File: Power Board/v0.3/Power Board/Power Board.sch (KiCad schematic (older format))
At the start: 3 parts, among them J1 Battery In, J2 Conn_01x06, SW1 SW_Push

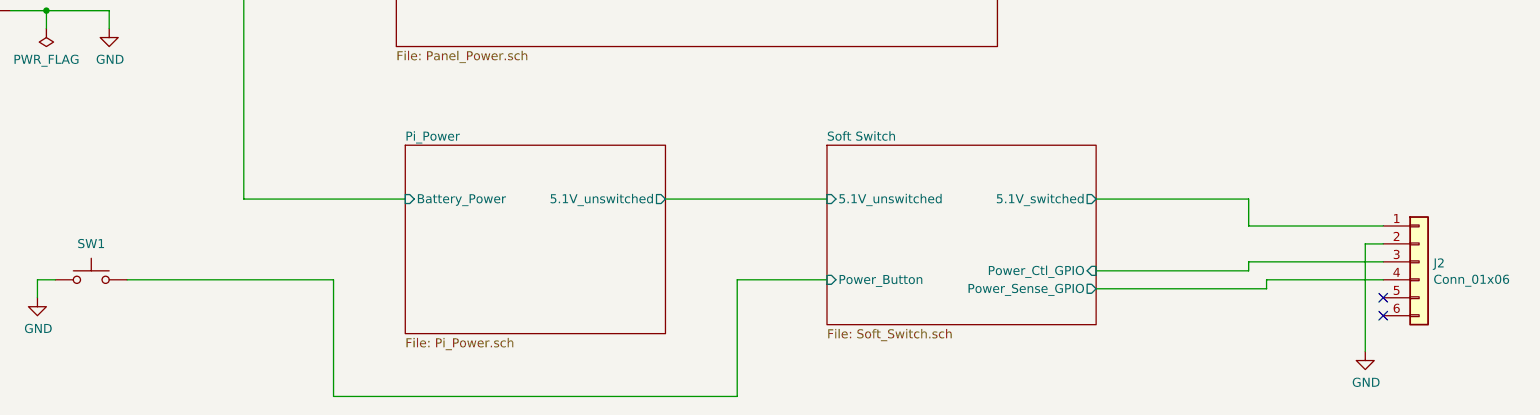
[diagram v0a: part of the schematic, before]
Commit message: Revised soft power switch.  Now switches power to 5V regulator.
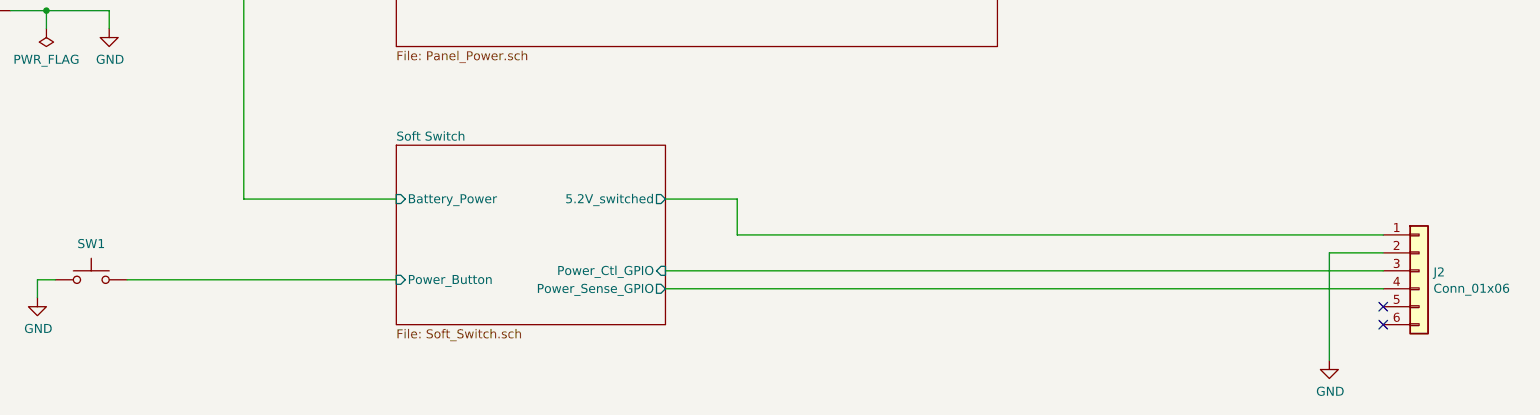
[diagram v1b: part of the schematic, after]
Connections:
- net Pi_Power/Battery_Power renamed Soft Switch/Battery_Power
- net Soft Switch/5.1V_switched renamed Soft Switch/5.2V_switched
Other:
- moved on the sheet: J2
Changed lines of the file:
@@
 	1    0    0    -1
 $EndComp
-$Sheet
-S 4150 3600 1450 1050
-U 5C93509D
-F0 "Pi_Power" 50
-F1 "Pi_Power.sch" 50
-F2 "Battery_Power" I L 4150 3900 50
-F3 "5.1V_unswitched" O R 5600 3900 50
-$EndSheet
-$Sheet
-S 6500 3600 1500 1000
-U 5C958DBD
-F0 "Soft Switch" 50
-F1 "Soft_Switch.sch" 50
-F2 "5.1V_unswitched" I L 6500 3900 50
-F3 "5.1V_switched" O R 8000 3900 50
-F4 "Power_Ctl_GPIO" I R 8000 4300 50
-F5 "Power_Sense_GPIO" O R 8000 4400 50
-F6 "Power_Button" I L 6500 4350 50
-$EndSheet
 $Comp
 L power:PWR_FLAG #FLG02
@@
 Wire Wire Line
 	3250 2750 3250 3900
-Wire Wire Line
-	3250 3900 4150 3900
 Connection ~ 2150 2750
 $Comp
@@
 Wire Wire Line
 	2100 4350 2100 4450
-Wire Wire Line
-	2600 4350 3750 4350
-Wire Wire Line
-	3750 4350 3750 5000
-Wire Wire Line
-	3750 5000 6000 5000
-Wire Wire Line
-	6000 5000 6000 4350
-Wire Wire Line
-	6000 4350 6500 4350
-Wire Wire Line
-	6500 3900 5600 3900
 $Comp
 L Connector_Generic:Conn_01x06 J2
 U 1 1 5C997D7E
-P 9800 4250
-F 0 "J2" H 9880 4242 50  0000 L CNN
-F 1 "Conn_01x06" H 9880 4151 50  0000 L CNN
-F 2 "" H 9800 4250 50  0001 C CNN
-F 3 "~" H 9800 4250 50  0001 C CNN
-F 4 "WM4904-ND" H 0   0   50  0001 C CNN "Digikey No."
-F 5 "Molex" H 0   0   50  0001 C CNN "Manufacturer"
-F 6 "70553-0005" H 0   0   50  0001 C CNN "Part No."
-	1    9800 4250
+P 9800 4300
+F 0 "J2" H 9880 4292 50  0000 L CNN
+F 1 "Conn_01x06" H 9880 4201 50  0000 L CNN
+F 2 "" H 9800 4300 50  0001 C CNN
+F 3 "~" H 9800 4300 50  0001 C CNN
+F 4 "WM4904-ND" H 0   50  50  0001 C CNN "Digikey No."
+F 5 "Molex" H 0   50  50  0001 C CNN "Manufacturer"
+F 6 "70553-0005" H 0   50  50  0001 C CNN "Part No."
+	1    9800 4300
 	1    0    0    -1
 $EndComp
 Wire Wire Line
-	9600 4050 8850 4050
+	9600 4100 6000 4100
 Wire Wire Line
-	8850 4050 8850 3900
+	9600 4200 9300 4200
 Wire Wire Line
-	8850 3900 8000 3900
-Wire Wire Line
-	8000 4300 8850 4300
-Wire Wire Line
-	8850 4300 8850 4250
-Wire Wire Line
-	8850 4250 9600 4250
-Wire Wire Line
-	8000 4400 8950 4400
-Wire Wire Line
-	8950 4400 8950 4350
-Wire Wire Line
-	8950 4350 9600 4350
-Wire Wire Line
-	9600 4150 9500 4150
-Wire Wire Line
-	9500 4150 9500 4750
+	9300 4200 9300 4800
 $Comp
 L power:GND #PWR03
 U 1 1 5C99AE97
-P 9500 4750
-F 0 "#PWR03" H 9500 4500 50  0001 C CNN
-F 1 "GND" H 9505 4577 50  0000 C CNN
-F 2 "" H 9500 4750 50  0001 C CNN
-F 3 "" H 9500 4750 50  0001 C CNN
-	1    9500 4750
+P 9300 4800
+F 0 "#PWR03" H 9300 4550 50  0001 C CNN
+F 1 "GND" H 9305 4627 50  0000 C CNN
+F 2 "" H 9300 4800 50  0001 C CNN
+F 3 "" H 9300 4800 50  0001 C CNN
+	1    9300 4800
 	1    0    0    -1
 $EndComp
-NoConn ~ 9600 4450
-NoConn ~ 9600 4550
+NoConn ~ 9600 4500
+NoConn ~ 9600 4600
+Wire Wire Line
+	6000 4100 6000 3900
+Wire Wire Line
+	6000 3900 5600 3900
+Wire Wire Line
+	5600 4400 9600 4400
+Wire Wire Line
+	9600 4300 5600 4300
+Wire Wire Line
+	4100 3900 3250 3900
+Wire Wire Line
+	2600 4350 4100 4350
+$Sheet
+S 4100 3600 1500 1000
+U 5C958DBD
+F0 "Soft Switch" 50
+F1 "Soft_Switch.sch" 50
+F2 "Power_Ctl_GPIO" I R 5600 4300 50
+F3 "Power_Sense_GPIO" O R 5600 4400 50
+F4 "Power_Button" I L 4100 4350 50
+F5 "5.2V_switched" O R 5600 3900 50
+F6 "Battery_Power" I L 4100 3900 50
+$EndSheet
 $EndSCHEMATC

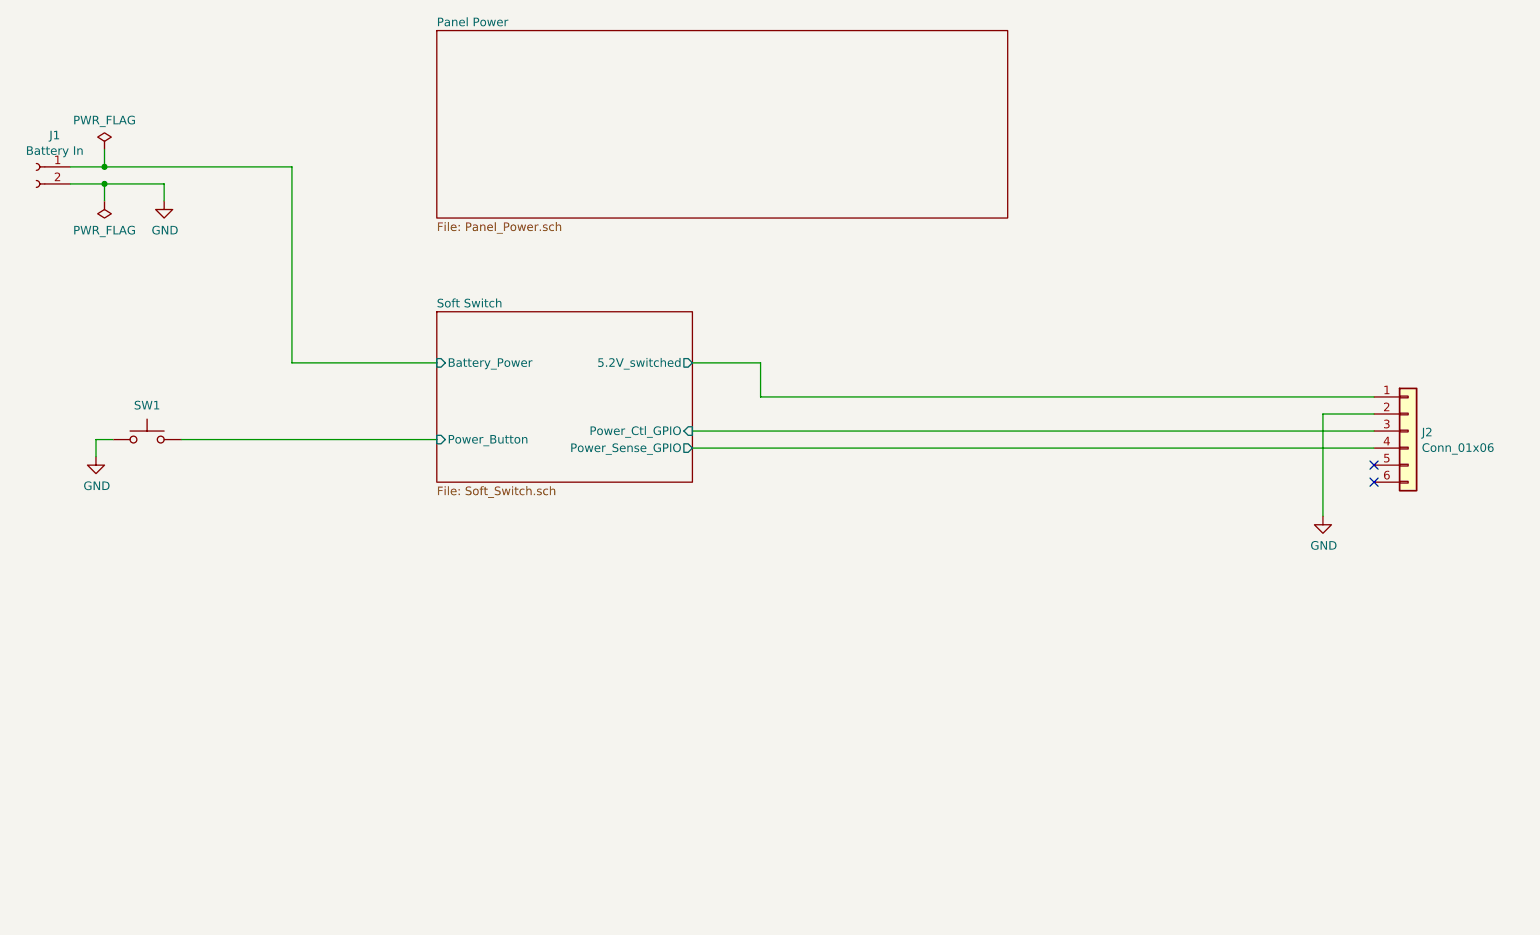
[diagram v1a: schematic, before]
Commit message: Merge Pi_Power schematic into Soft_Switch.
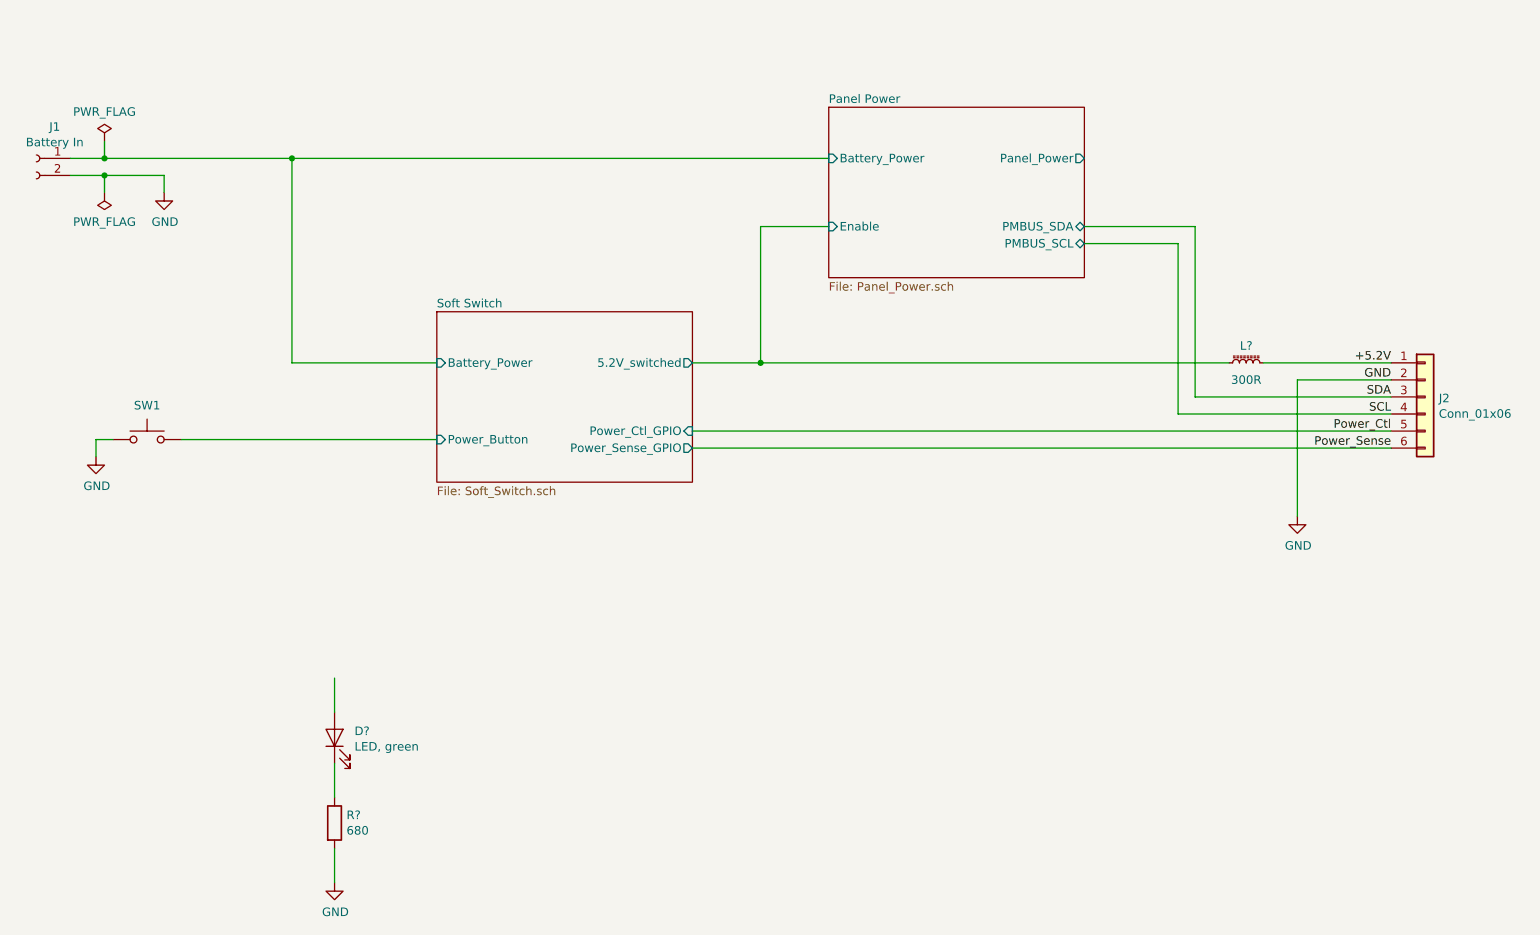
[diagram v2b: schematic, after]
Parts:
- added D?: LED, green, LED_SMD:LED_0603_1608Metric, symbol Device:LED
- added L?: 300R, Inductor_SMD:L_0603_1608Metric, symbol Device:L_Core_Ferrite_Small
- added R?: 680, Resistor_SMD:R_0603_1608Metric, symbol Device:R
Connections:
- net labels added: +5.2V, Power_Ctl, Power_Sense, SCL, SDA
- wire segments 19 -> 31
- no-connect marks 2 -> 0
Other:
- moved on the sheet: J1, J2
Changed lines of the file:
@@
 $Descr USLetter 11000 8500
 encoding utf-8
-Sheet 1 4
+Sheet 1 3
 Title "LED Cube Power Board"
 Date ""
@@
 L Connector:Conn_01x02_Female J1
 U 1 1 5C9104AD
-P 1750 2750
-F 0 "J1" H 1642 2935 50  0000 C CNN
-F 1 "Battery In" H 1642 2844 50  0000 C CNN
-F 2 "xxxx" H 1750 2750 50  0001 C CNN
-F 3 "https://www.molex.com/pdm_docs/sd/436500205_sd.pdf" H 1750 2750 50  0001 C CNN
-F 4 "WM17581-ND" H 0   0   50  0001 C CNN "Digikey No."
-F 5 "Molex" H 0   0   50  0001 C CNN "Manufacturer"
-F 6 "43650-0205" H 0   0   50  0001 C CNN "Part No."
-	1    1750 2750
+P 1750 2700
+F 0 "J1" H 1642 2885 50  0000 C CNN
+F 1 "Battery In" H 1642 2794 50  0000 C CNN
+F 2 "xxxx" H 1750 2700 50  0001 C CNN
+F 3 "https://www.molex.com/pdm_docs/sd/436500205_sd.pdf" H 1750 2700 50  0001 C CNN
+F 4 "WM17581-ND" H 0   -50 50  0001 C CNN "Digikey No."
+F 5 "Molex" H 0   -50 50  0001 C CNN "Manufacturer"
+F 6 "43650-0205" H 0   -50 50  0001 C CNN "Part No."
+	1    1750 2700
 	-1   0    0    -1
 $EndComp
@@
 L power:PWR_FLAG #FLG01
 U 1 1 5C912A06
-P 2150 2650
-F 0 "#FLG01" H 2150 2725 50  0001 C CNN
-F 1 "PWR_FLAG" H 2150 2823 50  0000 C CNN
-F 2 "" H 2150 2650 50  0001 C CNN
-F 3 "~" H 2150 2650 50  0001 C CNN
-	1    2150 2650
+P 2150 2600
+F 0 "#FLG01" H 2150 2675 50  0001 C CNN
+F 1 "PWR_FLAG" H 2150 2773 50  0000 C CNN
+F 2 "" H 2150 2600 50  0001 C CNN
+F 3 "~" H 2150 2600 50  0001 C CNN
+	1    2150 2600
 	1    0    0    -1
 $EndComp
@@
 L power:PWR_FLAG #FLG02
 U 1 1 5C9A6A29
-P 2150 2950
-F 0 "#FLG02" H 2150 3025 50  0001 C CNN
-F 1 "PWR_FLAG" H 2150 3123 50  0000 C CNN
-F 2 "" H 2150 2950 50  0001 C CNN
-F 3 "~" H 2150 2950 50  0001 C CNN
-	1    2150 2950
+P 2150 2900
+F 0 "#FLG02" H 2150 2975 50  0001 C CNN
+F 1 "PWR_FLAG" H 2150 3073 50  0000 C CNN
+F 2 "" H 2150 2900 50  0001 C CNN
+F 3 "~" H 2150 2900 50  0001 C CNN
+	1    2150 2900
 	-1   0    0    1
 $EndComp
 Wire Wire Line
-	1950 2850 2150 2850
-Wire Wire Line
-	2150 2850 2150 2950
-Wire Wire Line
-	1950 2750 2150 2750
-Wire Wire Line
-	2150 2750 2150 2650
-Wire Wire Line
-	2150 2850 2500 2850
-Wire Wire Line
-	2500 2850 2500 2950
-Connection ~ 2150 2850
+	1950 2800 2150 2800
+Wire Wire Line
+	2150 2800 2150 2900
+Wire Wire Line
+	1950 2700 2150 2700
+Wire Wire Line
+	2150 2700 2150 2600
+Wire Wire Line
+	2150 2800 2500 2800
+Wire Wire Line
+	2500 2800 2500 2900
+Connection ~ 2150 2800
 $Comp
 L power:GND #PWR02
 U 1 1 5C9A724E
-P 2500 2950
-F 0 "#PWR02" H 2500 2700 50  0001 C CNN
-F 1 "GND" H 2505 2777 50  0000 C CNN
-F 2 "" H 2500 2950 50  0001 C CNN
-F 3 "" H 2500 2950 50  0001 C CNN
-	1    2500 2950
+P 2500 2900
+F 0 "#PWR02" H 2500 2650 50  0001 C CNN
+F 1 "GND" H 2505 2727 50  0000 C CNN
+F 2 "" H 2500 2900 50  0001 C CNN
+F 3 "" H 2500 2900 50  0001 C CNN
+	1    2500 2900
 	1    0    0    -1
 $EndComp
 $Sheet
-S 4100 1950 3350 1100
+S 6400 2400 1500 1000
 U 5C9A7F1E
 F0 "Panel Power" 50
 F1 "Panel_Power.sch" 50
+F2 "Battery_Power" I L 6400 2700 50
+F3 "Enable" I L 6400 3100 50
+F4 "PMBUS_SCL" B R 7900 3200 50
+F5 "PMBUS_SDA" B R 7900 3100 50
+F6 "Panel_Power" O R 7900 2700 50
 $EndSheet
 Wire Wire Line
-	2150 2750 3250 2750
-Wire Wire Line
-	3250 2750 3250 3900
-Connection ~ 2150 2750
+	3250 2700 3250 3900
+Connection ~ 2150 2700
 $Comp
 L Switch:SW_Push SW1
@@
 L Connector_Generic:Conn_01x06 J2
 U 1 1 5C997D7E
-P 9800 4300
-F 0 "J2" H 9880 4292 50  0000 L CNN
-F 1 "Conn_01x06" H 9880 4201 50  0000 L CNN
-F 2 "" H 9800 4300 50  0001 C CNN
-F 3 "~" H 9800 4300 50  0001 C CNN
-F 4 "WM4904-ND" H 0   50  50  0001 C CNN "Digikey No."
-F 5 "Molex" H 0   50  50  0001 C CNN "Manufacturer"
-F 6 "70553-0005" H 0   50  50  0001 C CNN "Part No."
-	1    9800 4300
-	1    0    0    -1
-$EndComp
-Wire Wire Line
-	9600 4100 6000 4100
-Wire Wire Line
-	9600 4200 9300 4200
-Wire Wire Line
-	9300 4200 9300 4800
+P 9900 4100
+F 0 "J2" H 9980 4092 50  0000 L CNN
+F 1 "Conn_01x06" H 9980 4001 50  0000 L CNN
+F 2 "" H 9900 4100 50  0001 C CNN
+F 3 "~" H 9900 4100 50  0001 C CNN
+F 4 "WM4904-ND" H 100 -150 50  0001 C CNN "Digikey No."
+F 5 "Molex" H 100 -150 50  0001 C CNN "Manufacturer"
+F 6 "70553-0005" H 100 -150 50  0001 C CNN "Part No."
+	1    9900 4100
+	1    0    0    -1
+$EndComp
+Wire Wire Line
+	9700 3900 8950 3900
+Wire Wire Line
+	9700 4000 9150 4000
+Wire Wire Line
+	9150 4000 9150 4800
 $Comp
 L power:GND #PWR03
 U 1 1 5C99AE97
-P 9300 4800
-F 0 "#PWR03" H 9300 4550 50  0001 C CNN
-F 1 "GND" H 9305 4627 50  0000 C CNN
-F 2 "" H 9300 4800 50  0001 C CNN
-F 3 "" H 9300 4800 50  0001 C CNN
-	1    9300 4800
-	1    0    0    -1
-$EndComp
-NoConn ~ 9600 4500
-NoConn ~ 9600 4600
-Wire Wire Line
-	6000 4100 6000 3900
+P 9150 4800
+F 0 "#PWR03" H 9150 4550 50  0001 C CNN
+F 1 "GND" H 9155 4627 50  0000 C CNN
+F 2 "" H 9150 4800 50  0001 C CNN
+F 3 "" H 9150 4800 50  0001 C CNN
+	1    9150 4800
+	1    0    0    -1
+$EndComp
 Wire Wire Line
 	6000 3900 5600 3900
-Wire Wire Line
-	5600 4400 9600 4400
-Wire Wire Line
-	9600 4300 5600 4300
 Wire Wire Line
 	4100 3900 3250 3900
@@
 F6 "Battery_Power" I L 4100 3900 50
 $EndSheet
+Wire Wire Line
+	6000 3900 6000 3100
+Wire Wire Line
+	6000 3100 6400 3100
+Connection ~ 6000 3900
+Wire Wire Line
+	2150 2700 3250 2700
+Connection ~ 3250 2700
+Wire Wire Line
+	3250 2700 6400 2700
+Wire Wire Line
+	7900 3100 8550 3100
+Wire Wire Line
+	8550 3100 8550 4100
+Wire Wire Line
+	8450 4200 8450 3200
+$Comp
+L Device:L_Core_Ferrite_Small L?
+U 1 1 5CC268DC
+P 8850 3900
+AR Path="/5C958DBD/5CC268DC" Ref="L?"  Part="1"
+AR Path="/5CC268DC" Ref="L?"  Part="1"
+F 0 "L?" V 8950 3900 50  0000 C CNN
+F 1 "300R" V 8750 3900 50  0000 C CNN
+F 2 "Inductor_SMD:L_0603_1608Metric" H 8850 3900 50  0001 C CNN
+F 3 "https://www.niccomp.com/catalog/ncbh.pdf" H 8850 3900 50  0001 C CNN
+F 4 "not avail." H 1600 950 50  0001 C CNN "Digikey No."
+F 5 "NIC" H 1600 950 50  0001 C CNN "Manufacturer"
+F 6 "NCB-H0603R301TR100F" H 1600 950 50  0001 C CNN "Part No."
+	1    8850 3900
+	0    -1   -1   0
+$EndComp
+Wire Wire Line
+	9700 4300 5600 4300
+Wire Wire Line
+	5600 4400 9700 4400
+Wire Wire Line
+	8450 4200 9700 4200
+Wire Wire Line
+	9700 4100 8550 4100
+Text Label 9700 3900 2    50   ~ 0
++5.2V
+Text Label 9700 4000 2    50   ~ 0
+GND
+Text Label 9700 4100 2    50   ~ 0
+SDA
+Text Label 9700 4200 2    50   ~ 0
+SCL
+Text Label 9700 4300 2    50   ~ 0
+Power_Ctl
+Text Label 9700 4400 2    50   ~ 0
+Power_Sense
+Wire Wire Line
+	8450 3200 7900 3200
+Wire Wire Line
+	8750 3900 6000 3900
+Wire Wire Line
+	3500 5950 3500 5750
+Wire Wire Line
+	3500 6250 3500 6450
+Wire Wire Line
+	3500 6750 3500 6950
+$Comp
+L power:GND #PWR?
+U 1 1 5CC4DF21
+P 3500 6950
+AR Path="/5C958DBD/5CC4DF21" Ref="#PWR?"  Part="1"
+AR Path="/5CC4DF21" Ref="#PWR?"  Part="1"
+F 0 "#PWR?" H 3500 6700 50  0001 C CNN
+F 1 "GND" H 3505 6777 50  0000 C CNN
+F 2 "" H 3500 6950 50  0001 C CNN
+F 3 "" H 3500 6950 50  0001 C CNN
+	1    3500 6950
+	1    0    0    -1
+$EndComp
+$Comp
+L Device:R R?
+U 1 1 5CC4DF29
+P 3500 6600
+AR Path="/5C958DBD/5CC4DF29" Ref="R?"  Part="1"
+AR Path="/5CC4DF29" Ref="R?"  Part="1"
+F 0 "R?" H 3570 6646 50  0000 L CNN
+F 1 "680" H 3570 6555 50  0000 L CNN
+F 2 "Resistor_SMD:R_0603_1608Metric" V 3430 6600 50  0001 C CNN
+F 3 "~" H 3500 6600 50  0001 C CNN
+F 4 "Yageo" H -3900 2800 50  0001 C CNN "Manufacturer"
+F 5 "RC0603JR-07680R" H -3900 2800 50  0001 C CNN "Part No."
+	1    3500 6600
+	1    0    0    -1
+$EndComp
+$Comp
+L Device:LED D?
+U 1 1 5CC4DF31
+P 3500 6100
+AR Path="/5C958DBD/5CC4DF31" Ref="D?"  Part="1"
+AR Path="/5CC4DF31" Ref="D?"  Part="1"
+F 0 "D?" V 3539 5983 50  0000 R CNN
+F 1 "LED, green" V 3448 5983 50  0000 R CNN
+F 2 "LED_SMD:LED_0603_1608Metric" H 3500 6100 50  0001 C CNN
+F 3 "~" H 3500 6100 50  0001 C CNN
+F 4 "Osram" H -3900 2800 50  0001 C CNN "Manufacturer"
+F 5 "LG Q971-KN-1" H -3900 2800 50  0001 C CNN "Part No."
+	1    3500 6100
+	0    -1   -1   0
+$EndComp
 $EndSCHEMATC
